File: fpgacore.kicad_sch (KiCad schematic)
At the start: 10 parts, among them U6 XC7A35T-FGG484

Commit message: Add LCSC Basic/Extended part numbers for JLC-placed passives and ferrite beads
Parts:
- C79, C80: LCSC Part (none) -> C107368
- C81, C82, C83, C84: LCSC Part (none) -> C14663
- FB1, FB2: LCSC Part (none) -> C19330
- R17: LCSC Part (none) -> C2906981
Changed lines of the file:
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@@
 			)
 		)
+		(property "LCSC Part" "C14663"
+			(at 0 0 0)
+			(hide yes)
+			(show_name no)
+			(do_not_autoplace no)
+			(effects
+				(font
+					(size 1.27 1.27)
+				)
+			)
+		)
 		(property "Datasheet" ""
 			(at 241.3 38.1 0)
@@
 			)
 		)
+		(property "LCSC Part" "C19330"
+			(at 0 0 0)
+			(hide yes)
+			(show_name no)
+			(do_not_autoplace no)
+			(effects
+				(font
+					(size 1.27 1.27)
+				)
+			)
+		)
 		(property "Datasheet" ""
 			(at 45.72 57.15 0)
@@
 			)
 		)
+		(property "LCSC Part" "C14663"
+			(at 0 0 0)
+			(hide yes)
+			(show_name no)
+			(do_not_autoplace no)
+			(effects
+				(font
+					(size 1.27 1.27)
+				)
+			)
+		)
 		(property "Datasheet" ""
 			(at 228.6 38.1 0)
@@
 			)
 		)
+		(property "LCSC Part" "C14663"
+			(at 0 0 0)
+			(hide yes)
+			(show_name no)
+			(do_not_autoplace no)
+			(effects
+				(font
+					(size 1.27 1.27)
+				)
+			)
+		)
 		(property "Datasheet" ""
 			(at 193.04 39.37 0)
@@
 			)
 		)
+		(property "LCSC Part" "C107368"
+			(at 0 0 0)
+			(hide yes)
+			(show_name no)
+			(do_not_autoplace no)
+			(effects
+				(font
+					(size 1.27 1.27)
+				)
+			)
+		)
 		(property "Datasheet" ""
 			(at 167.64 39.37 0)
@@
 			)
 		)
+		(property "LCSC Part" "C2906981"
+			(at 0 0 0)
+			(hide yes)
+			(show_name no)
+			(do_not_autoplace no)
+			(effects
+				(font
+					(size 1.27 1.27)
+				)
+			)
+		)
 		(property "Datasheet" ""
 			(at 151.13 116.84 0)
@@
 			)
 		)
+		(property "LCSC Part" "C14663"
+			(at 0 0 0)
+			(hide yes)
+			(show_name no)
+			(do_not_autoplace no)
+			(effects
+				(font
+					(size 1.27 1.27)
+				)
+			)
+		)
 		(property "Datasheet" ""
 			(at 180.34 39.37 0)
@@
 			)
 		)
+		(property "LCSC Part" "C19330"
+			(at 0 0 0)
+			(hide yes)
+			(show_name no)
+			(do_not_autoplace no)
+			(effects
+				(font
+					(size 1.27 1.27)
+				)
+			)
+		)
 		(property "Datasheet" ""
 			(at 88.9 57.15 0)
@@
 			(hide yes)
 			(show_name no)
+			(do_not_autoplace no)
+			(effects
+				(font
+					(size 1.27 1.27)
+				)
+			)
+		)
+		(property "LCSC Part" "C107368"
+			(at 0 0 0)
+			(hide yes)
+			(show_name no)

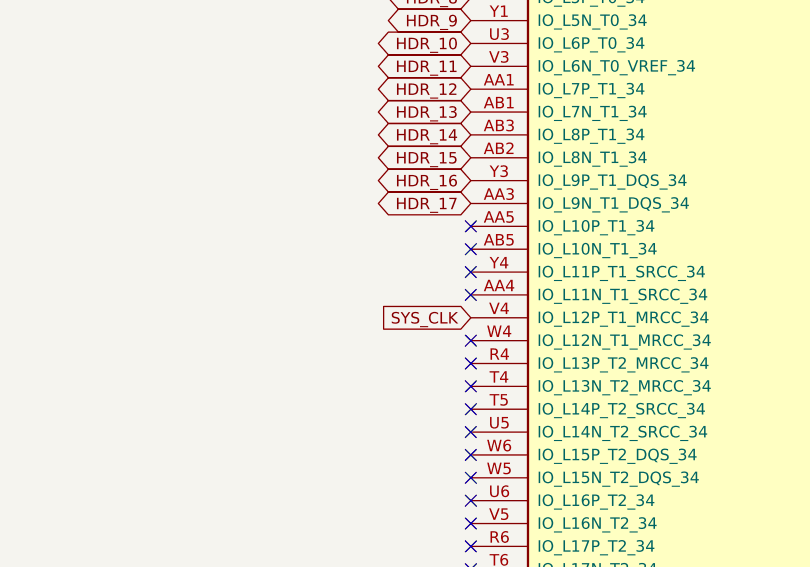
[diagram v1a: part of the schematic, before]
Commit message: Add optional ESP32-C3 WiFi sheet, convert hand-solder parts to through-hole
- New wifi sheet: ESP32-C3-MINI-1 module on SPI to spare FPGA bank 34, with EN/boot-strap networks, 3V3 bypass/bulk caps and a UART debug header
- Replace SMD hand-solder resistors, LEDs, zener, fuse and ceramic caps with THT equivalents; bulk 10uF/22uF caps become polarized electrolytics
- Fill in LCSC part numbers for the new parts and regenerate BOM and ERC report
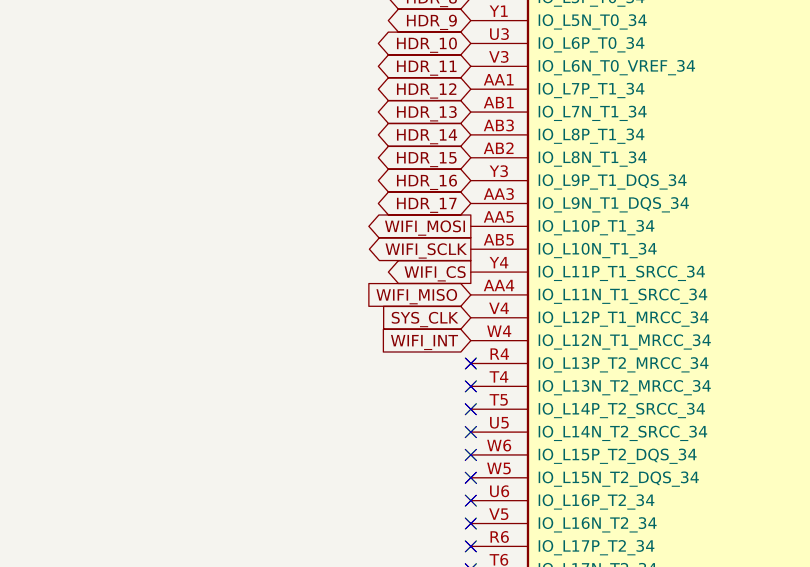
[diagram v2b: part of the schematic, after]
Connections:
- net WIFI_MISO: now reaches U6.AA4 (IO_L11N_T1_SRCC_34)
- net WIFI_MOSI: now reaches U6.AA5 (IO_L10P_T1_34)
- net WIFI_SCLK: now reaches U6.AB5 (IO_L10N_T1_34)
- net WIFI_INT: now reaches U6.W4 (IO_L12N_T1_MRCC_34)
- net WIFI_CS: now reaches U6.Y4 (IO_L11P_T1_SRCC_34)
- no-connect marks 212 -> 207
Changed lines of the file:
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@@
 	)
 	(no_connect
-		(at 269.24 318.77)
-	)
-	(no_connect
 		(at 554.99 140.97)
 	)
@@
 	)
 	(no_connect
-		(at 269.24 311.15)
-	)
-	(no_connect
 		(at 453.39 118.11)
 	)
@@
 	)
 	(no_connect
-		(at 269.24 308.61)
-	)
-	(no_connect
 		(at 433.07 247.65)
 	)
@@
 	)
 	(no_connect
-		(at 269.24 313.69)
-	)
-	(no_connect
 		(at 453.39 82.55)
 	)
@@
 	)
 	(no_connect
-		(at 269.24 306.07)
-	)
-	(no_connect
 		(at 453.39 151.13)
 	)
@@
 		)
 	)
+	(global_label "WIFI_INT"
+		(shape input)
+		(at 269.24 318.77 180)
+		(fields_autoplaced yes)
+		(effects
+			(font
+				(size 1.27 1.27)
+			)
+			(justify right)
+		)
+		(property "Intersheetrefs" "${INTERSHEET_REFS}"
+			(at 258.6347 318.77 0)
+			(hide yes)
+			(show_name no)
+			(do_not_autoplace no)
+			(effects
+				(font
+					(size 1.27 1.27)
+				)
+				(justify right)
+			)
+		)
+	)
 	(global_label "3V3"
 		(shape input)
@@
 		)
 	)
+	(global_label "WIFI_SCLK"
+		(shape output)
+		(at 269.24 308.61 180)
+		(fields_autoplaced yes)
+		(effects
+			(font
+				(size 1.27 1.27)
+			)
+			(justify right)
+		)
+		(property "Intersheetrefs" "${INTERSHEET_REFS}"
+			(at 256.76 308.61 0)
+			(hide yes)
+			(show_name no)
+			(do_not_autoplace no)
+			(effects
+				(font
+					(size 1.27 1.27)
+				)
+				(justify right)
+			)
+		)
+	)
 	(global_label "SFP_RX_P"
 		(shape input)
@@
 		)
 	)
+	(global_label "WIFI_MOSI"
+		(shape output)
+		(at 269.24 306.07 180)
+		(fields_autoplaced yes)
+		(effects
+			(font
+				(size 1.27 1.27)
+			)
+			(justify right)
+		)
+		(property "Intersheetrefs" "${INTERSHEET_REFS}"
+			(at 256.9414 306.07 0)
+			(hide yes)
+			(show_name no)
+			(do_not_autoplace no)
+			(effects
+				(font
+					(size 1.27 1.27)
+				)
+				(justify right)
+			)
+		)
+	)
 	(global_label "HDR_15"
 		(shape bidirectional)
@@
 		)
 	)
+	(global_label "WIFI_MISO"
+		(shape input)
+		(at 269.24 313.69 180)
+		(fields_autoplaced yes)
+		(effects
+			(font
+				(size 1.27 1.27)
+			)
+			(justify right)
+		)
+		(property "Intersheetrefs" "${INTERSHEET_REFS}"
+			(at 256.9414 313.69 0)
+			(hide yes)
+			(show_name no)
+			(do_not_autoplace no)
+			(effects
+				(font
+					(size 1.27 1.27)
+				)
+				(justify right)
+			)
+		)
+	)
 	(global_label "CFG_CCLK"
 		(shape bidirectional)
@@
 		)
 	)
+	(global_label "WIFI_CS"
+		(shape output)
+		(at 269.24 311.15 180)
+		(fields_autoplaced yes)
+		(effects
+			(font
+				(size 1.27 1.27)
+			)
+			(justify right)
+		)
+		(property "Intersheetrefs" "${INTERSHEET_REFS}"
+			(at 259.0581 311.15 0)
+			(hide yes)
+			(show_name no)
+			(do_not_autoplace no)
+			(effects
+				(font
+					(size 1.27 1.27)
+				)
+				(justify right)
+			)
+		)
+	)
 	(global_label "LED2"
 		(shape output)
@@
 			)
 		)
-		(property "LCSC Part" "C14663"
-			(at 0 0 0)
+		(property "Datasheet" ""
+			(at 241.3 38.1 0)
 			(hide yes)
 			(show_name no)
@@
 			)
 		)
-		(property "Datasheet" ""
+		(property "Description" "Unpolarized capacitor"
 			(at 241.3 38.1 0)
 			(hide yes)
@@
 			)
 		)
-		(property "Description" "Unpolarized capacitor"
-			(at 241.3 38.1 0)
+		(property "LCSC Part" "C14663"
+			(at 0 0 0)
 			(hide yes)
 			(show_name no)
@@
 			)
 		)
-		(property "LCSC Part" "C19330"
-			(at 0 0 0)
+		(property "Datasheet" ""
+			(at 45.72 57.15 0)
 			(hide yes)
 			(show_name no)
@@
 			)
 		)
-		(property "Datasheet" ""
+		(property "Description" "Ferrite bead"
 			(at 45.72 57.15 0)
 			(hide yes)
@@
 			)
 		)
-		(property "Description" "Ferrite bead"
-			(at 45.72 57.15 0)
+		(property "LCSC Part" "C19330"
+			(at 0 0 0)
 			(hide yes)
 			(show_name no)
@@
 			)
 		)
-		(property "LCSC Part" "C14663"
-			(at 0 0 0)
+		(property "Datasheet" ""
+			(at 228.6 38.1 0)
 			(hide yes)
 			(show_name no)
@@
 			)
 		)
-		(property "Datasheet" ""
+		(property "Description" "Unpolarized capacitor"
 			(at 228.6 38.1 0)
 			(hide yes)
@@
 			)
 		)
-		(property "Description" "Unpolarized capacitor"
-			(at 228.6 38.1 0)
+		(property "LCSC Part" "C14663"
+			(at 0 0 0)
 			(hide yes)
 			(show_name no)
@@
 			)
 		)
-		(property "LCSC Part" "C14663"
-			(at 0 0 0)
+		(property "Datasheet" ""
+			(at 193.04 39.37 0)
 			(hide yes)
 			(show_name no)
@@
 			)
 		)
-		(property "Datasheet" ""
+		(property "Description" "Unpolarized capacitor"
 			(at 193.04 39.37 0)
 			(hide yes)
@@
 			)
 		)
-		(property "Description" "Unpolarized capacitor"
-			(at 193.04 39.37 0)
+		(property "LCSC Part" "C14663"
+			(at 0 0 0)
 			(hide yes)
 			(show_name no)
@@
 			)
 		)
-		(property "LCSC Part" "C107368"
-			(at 0 0 0)
+		(property "Datasheet" ""
+			(at 167.64 39.37 0)
 			(hide yes)
 			(show_name no)
@@
 			)
 		)
-		(property "Datasheet" ""
+		(property "Description" "Unpolarized capacitor"
 			(at 167.64 39.37 0)
 			(hide yes)
@@
 			)
 		)
-		(property "Description" "Unpolarized capacitor"
-			(at 167.64 39.37 0)
+		(property "LCSC Part" "C107368"
+			(at 0 0 0)
 			(hide yes)
 			(show_name no)
@@
 			)
 		)
-		(property "LCSC Part" "C2906981"
-			(at 0 0 0)
+		(property "Datasheet" ""
+			(at 151.13 116.84 0)
 			(hide yes)
 			(show_name no)
@@
 			)
 		)
-		(property "Datasheet" ""
+		(property "Description" "Resistor"
 			(at 151.13 116.84 0)
 			(hide yes)
@@
 			)
 		)
-		(property "Description" "Resistor"
-			(at 151.13 116.84 0)
+		(property "LCSC Part" "C2906981"
+			(at 0 0 0)
 			(hide yes)
 			(show_name no)
@@
 			)
 		)
-		(property "LCSC Part" "C14663"
-			(at 0 0 0)
+		(property "Datasheet" ""
+			(at 180.34 39.37 0)
 			(hide yes)
 			(show_name no)
@@
 			)
 		)
-		(property "Datasheet" ""
+		(property "Description" "Unpolarized capacitor"
 			(at 180.34 39.37 0)
 			(hide yes)
@@
 			)
 		)
-		(property "Description" "Unpolarized capacitor"
-			(at 180.34 39.37 0)
+		(property "LCSC Part" "C14663"
+			(at 0 0 0)
 			(hide yes)
 			(show_name no)
@@
 			)
 		)
-		(property "LCSC Part" "C19330"
-			(at 0 0 0)
+		(property "Datasheet" ""
+			(at 88.9 57.15 0)
 			(hide yes)
 			(show_name no)
@@
 			)
 		)
-		(property "Datasheet" ""
+		(property "Description" "Ferrite bead"
 			(at 88.9 57.15 0)
 			(hide yes)
@@
 			)
 		)
-		(property "Description" "Ferrite bead"
-			(at 88.9 57.15 0)
+		(property "LCSC Part" "C19330"
+			(at 0 0 0)
 			(hide yes)
 			(show_name no)
@@
 			)
 		)
-		(property "LCSC Part" "C107368"
-			(at 0 0 0)
+		(property "Datasheet" ""
+			(at 215.9 38.1 0)
 			(hide yes)
 			(show_name no)
@@
 			)
 		)
-		(property "Datasheet" ""
+		(property "Description" "Unpolarized capacitor"
 			(at 215.9 38.1 0)
 			(hide yes)
@@
 			)
 		)
-		(property "Description" "Unpolarized capacitor"
-			(at 215.9 38.1 0)
+		(property "LCSC Part" "C107368"
+			(at 0 0 0)
 			(hide yes)
 			(show_name no)

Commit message: Remove optional WiFi sheet from schematic and PCB
- Delete wifi sheet and its seven parts; restore no-connect flags on the five freed FPGA bank-34 pins
- Reduce J4 pad solder-mask margin so the fine-pitch pads meet the 0.1mm web rule
- Regenerate BOM and ERC report
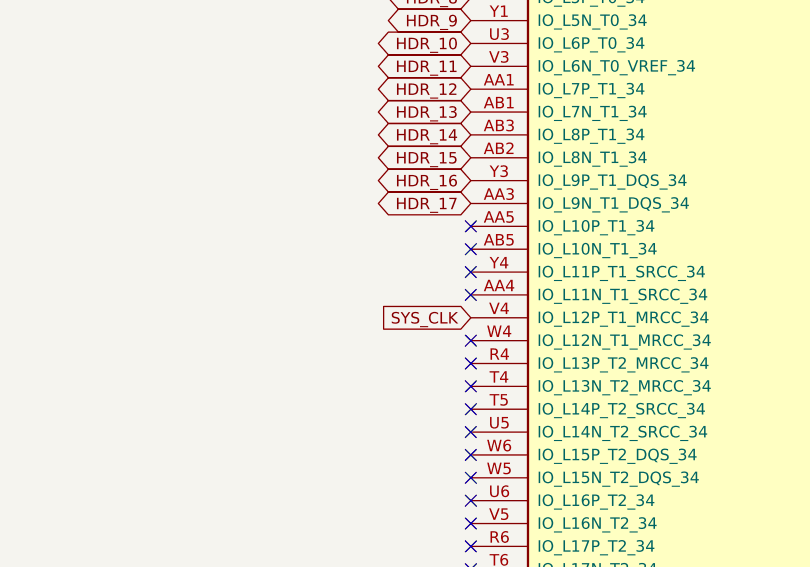
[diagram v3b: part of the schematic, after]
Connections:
- net WIFI_CS: no longer names the net of U6.Y4 (IO_L11P_T1_SRCC_34)
- net WIFI_INT: no longer names the net of U6.W4 (IO_L12N_T1_MRCC_34)
- net WIFI_MISO: no longer names the net of U6.AA4 (IO_L11N_T1_SRCC_34)
- net WIFI_MOSI: no longer names the net of U6.AA5 (IO_L10P_T1_34)
- net WIFI_SCLK: no longer names the net of U6.AB5 (IO_L10N_T1_34)
- no-connect marks 207 -> 212
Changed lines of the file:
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@@
 	)
 	(no_connect
+		(at 269.24 318.77)
+	)
+	(no_connect
 		(at 554.99 140.97)
 	)
@@
 	)
 	(no_connect
+		(at 269.24 311.15)
+	)
+	(no_connect
 		(at 453.39 118.11)
 	)
@@
 	)
 	(no_connect
+		(at 269.24 308.61)
+	)
+	(no_connect
 		(at 433.07 247.65)
 	)
@@
 	)
 	(no_connect
+		(at 269.24 313.69)
+	)
+	(no_connect
 		(at 453.39 82.55)
 	)
@@
 	)
 	(no_connect
+		(at 269.24 306.07)
+	)
+	(no_connect
 		(at 453.39 151.13)
 	)
@@
 		)
 	)
-	(global_label "WIFI_INT"
-		(shape input)
-		(at 269.24 318.77 180)
-		(fields_autoplaced yes)
-		(effects
-			(font
-				(size 1.27 1.27)
-			)
-			(justify right)
-		)
-		(property "Intersheetrefs" "${INTERSHEET_REFS}"
-			(at 258.6347 318.77 0)
-			(hide yes)
-			(show_name no)
-			(do_not_autoplace no)
-			(effects
-				(font
-					(size 1.27 1.27)
-				)
-				(justify right)
-			)
-		)
-	)
 	(global_label "3V3"
 		(shape input)
@@
 		)
 	)
-	(global_label "WIFI_SCLK"
-		(shape output)
-		(at 269.24 308.61 180)
-		(fields_autoplaced yes)
-		(effects
-			(font
-				(size 1.27 1.27)
-			)
-			(justify right)
-		)
-		(property "Intersheetrefs" "${INTERSHEET_REFS}"
-			(at 256.76 308.61 0)
-			(hide yes)
-			(show_name no)
-			(do_not_autoplace no)
-			(effects
-				(font
-					(size 1.27 1.27)
-				)
-				(justify right)
-			)
-		)
-	)
 	(global_label "SFP_RX_P"
 		(shape input)
@@
 		)
 	)
-	(global_label "WIFI_MOSI"
-		(shape output)
-		(at 269.24 306.07 180)
-		(fields_autoplaced yes)
-		(effects
-			(font
-				(size 1.27 1.27)
-			)
-			(justify right)
-		)
-		(property "Intersheetrefs" "${INTERSHEET_REFS}"
-			(at 256.9414 306.07 0)
-			(hide yes)
-			(show_name no)
-			(do_not_autoplace no)
-			(effects
-				(font
-					(size 1.27 1.27)
-				)
-				(justify right)
-			)
-		)
-	)
 	(global_label "HDR_15"
 		(shape bidirectional)
@@
 		)
 	)
-	(global_label "WIFI_MISO"
-		(shape input)
-		(at 269.24 313.69 180)
-		(fields_autoplaced yes)
-		(effects
-			(font
-				(size 1.27 1.27)
-			)
-			(justify right)
-		)
-		(property "Intersheetrefs" "${INTERSHEET_REFS}"
-			(at 256.9414 313.69 0)
-			(hide yes)
-			(show_name no)
-			(do_not_autoplace no)
-			(effects
-				(font
-					(size 1.27 1.27)
-				)
-				(justify right)
-			)
-		)
-	)
 	(global_label "CFG_CCLK"
 		(shape bidirectional)
@@
 		)
 	)
-	(global_label "WIFI_CS"
-		(shape output)
-		(at 269.24 311.15 180)
-		(fields_autoplaced yes)
-		(effects
-			(font
-				(size 1.27 1.27)
-			)
-			(justify right)
-		)
-		(property "Intersheetrefs" "${INTERSHEET_REFS}"
-			(at 259.0581 311.15 0)
-			(hide yes)
-			(show_name no)
-			(do_not_autoplace no)
-			(effects
-				(font
-					(size 1.27 1.27)
-				)
-				(justify right)
-			)
-		)
-	)
 	(global_label "LED2"
 		(shape output)
@@
 			)
 		)
-		(property "Datasheet" ""
-			(at 241.3 38.1 0)
+		(property "LCSC Part" "C14663"
+			(at 0 0 0)
 			(hide yes)
 			(show_name no)
@@
 			)
 		)
-		(property "Description" "Unpolarized capacitor"
+		(property "Datasheet" ""
 			(at 241.3 38.1 0)
 			(hide yes)
@@
 			)
 		)
-		(property "LCSC Part" "C14663"
-			(at 0 0 0)
+		(property "Description" "Unpolarized capacitor"
+			(at 241.3 38.1 0)
 			(hide yes)
 			(show_name no)
@@
 			)
 		)
-		(property "Datasheet" ""
-			(at 45.72 57.15 0)
+		(property "LCSC Part" "C19330"
+			(at 0 0 0)
 			(hide yes)
 			(show_name no)
@@
 			)
 		)
-		(property "Description" "Ferrite bead"
+		(property "Datasheet" ""
 			(at 45.72 57.15 0)
 			(hide yes)
@@
 			)
 		)
-		(property "LCSC Part" "C19330"
-			(at 0 0 0)
+		(property "Description" "Ferrite bead"
+			(at 45.72 57.15 0)
 			(hide yes)
 			(show_name no)
@@
 			)
 		)
-		(property "Datasheet" ""
-			(at 228.6 38.1 0)
+		(property "LCSC Part" "C14663"
+			(at 0 0 0)
 			(hide yes)
 			(show_name no)
@@
 			)
 		)
-		(property "Description" "Unpolarized capacitor"
+		(property "Datasheet" ""
 			(at 228.6 38.1 0)
 			(hide yes)
@@
 			)
 		)
-		(property "LCSC Part" "C14663"
-			(at 0 0 0)
+		(property "Description" "Unpolarized capacitor"
+			(at 228.6 38.1 0)
 			(hide yes)
 			(show_name no)
@@
 			)
 		)
-		(property "Datasheet" ""
-			(at 193.04 39.37 0)
+		(property "LCSC Part" "C14663"
+			(at 0 0 0)
 			(hide yes)
 			(show_name no)
@@
 			)
 		)
-		(property "Description" "Unpolarized capacitor"
+		(property "Datasheet" ""
 			(at 193.04 39.37 0)
 			(hide yes)
@@
 			)
 		)
-		(property "LCSC Part" "C14663"
-			(at 0 0 0)
+		(property "Description" "Unpolarized capacitor"
+			(at 193.04 39.37 0)
 			(hide yes)
 			(show_name no)
@@
 			)
 		)
-		(property "Datasheet" ""
-			(at 167.64 39.37 0)
+		(property "LCSC Part" "C107368"
+			(at 0 0 0)
 			(hide yes)
 			(show_name no)
@@
 			)
 		)
-		(property "Description" "Unpolarized capacitor"
+		(property "Datasheet" ""
 			(at 167.64 39.37 0)
 			(hide yes)
@@
 			)
 		)
-		(property "LCSC Part" "C107368"
-			(at 0 0 0)
+		(property "Description" "Unpolarized capacitor"
+			(at 167.64 39.37 0)
 			(hide yes)
 			(show_name no)
@@
 			)
 		)
-		(property "Datasheet" ""
-			(at 151.13 116.84 0)
+		(property "LCSC Part" "C2906981"
+			(at 0 0 0)
 			(hide yes)
 			(show_name no)
@@
 			)
 		)
-		(property "Description" "Resistor"
+		(property "Datasheet" ""
 			(at 151.13 116.84 0)
 			(hide yes)
@@
 			)
 		)
-		(property "LCSC Part" "C2906981"
-			(at 0 0 0)
+		(property "Description" "Resistor"
+			(at 151.13 116.84 0)
 			(hide yes)
 			(show_name no)
@@
 			)
 		)
-		(property "Datasheet" ""
-			(at 180.34 39.37 0)
+		(property "LCSC Part" "C14663"
+			(at 0 0 0)
 			(hide yes)
 			(show_name no)
@@
 			)
 		)
-		(property "Description" "Unpolarized capacitor"
+		(property "Datasheet" ""
 			(at 180.34 39.37 0)
 			(hide yes)
@@
 			)
 		)
-		(property "LCSC Part" "C14663"
-			(at 0 0 0)
+		(property "Description" "Unpolarized capacitor"
+			(at 180.34 39.37 0)
 			(hide yes)
 			(show_name no)
@@
 			)
 		)
-		(property "Datasheet" ""
-			(at 88.9 57.15 0)
+		(property "LCSC Part" "C19330"
+			(at 0 0 0)
 			(hide yes)
 			(show_name no)
@@
 			)
 		)
-		(property "Description" "Ferrite bead"
+		(property "Datasheet" ""
 			(at 88.9 57.15 0)
 			(hide yes)
@@
 			)
 		)
-		(property "LCSC Part" "C19330"
-			(at 0 0 0)
+		(property "Description" "Ferrite bead"
+			(at 88.9 57.15 0)
 			(hide yes)
 			(show_name no)
@@
 			)
 		)
-		(property "Datasheet" ""
-			(at 215.9 38.1 0)
+		(property "LCSC Part" "C107368"
+			(at 0 0 0)
 			(hide yes)
 			(show_name no)
@@
 			)
 		)
-		(property "Description" "Unpolarized capacitor"
+		(property "Datasheet" ""
 			(at 215.9 38.1 0)
 			(hide yes)
@@
 			)
 		)
-		(property "LCSC Part" "C107368"
-			(at 0 0 0)
+		(property "Description" "Unpolarized capacitor"
+			(at 215.9 38.1 0)
 			(hide yes)
 			(show_name no)
